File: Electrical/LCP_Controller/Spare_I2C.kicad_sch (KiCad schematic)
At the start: 4 parts, among them Q2 TSM500P02CX RFG

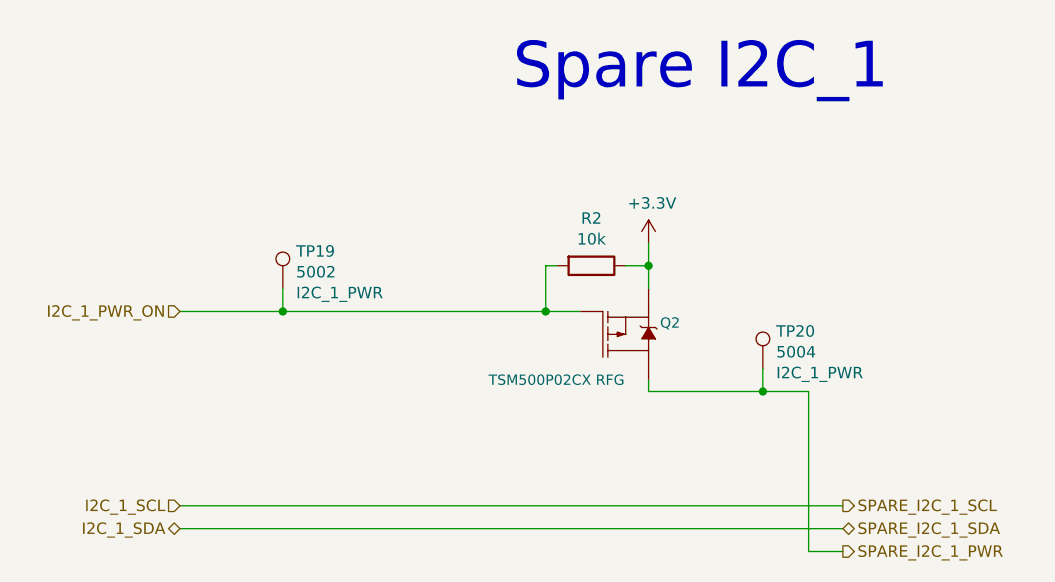
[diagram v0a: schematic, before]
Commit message: Hardware Revision : v0.3
1. modified schematic design, removed unnecessary test points.
2. pcb layout 2x8 Inches allowance dimension, layout is in progress
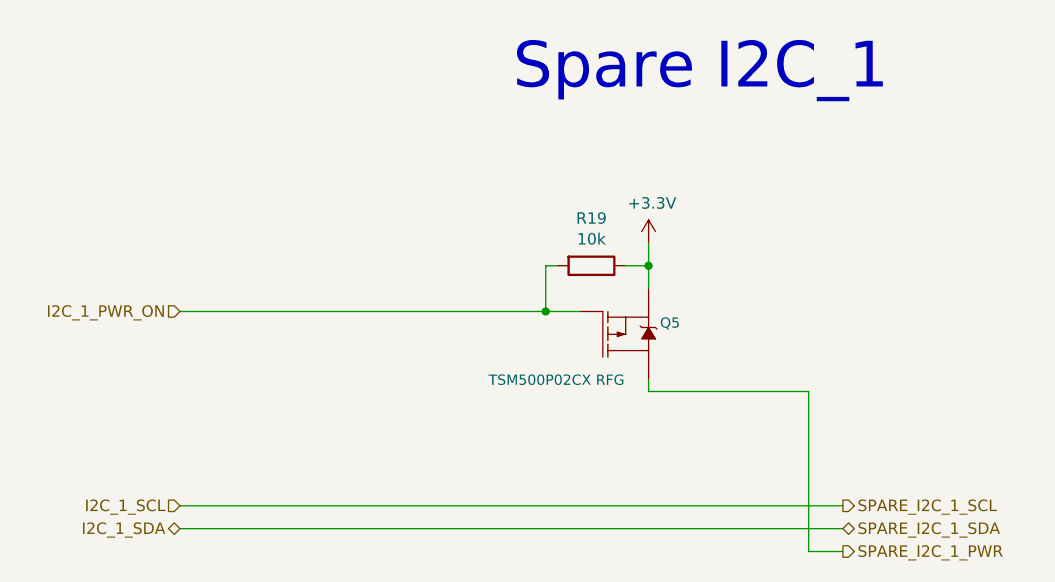
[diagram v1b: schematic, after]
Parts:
- removed TP19: 5002, TestPoint:TestPoint_Keystone_5000-5004_Miniature, symbol Connector:TestPoint
- removed TP20: 5004, TestPoint:TestPoint_Keystone_5000-5004_Miniature, symbol Connector:TestPoint
- renumbered Q2 to Q5, R2 to R19
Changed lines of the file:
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@@
   (junction (at 124.46 91.44) (diameter 0) (color 0 0 0 0)
-  )
-  (junction (at 95.25 91.44) (diameter 0) (color 0 0 0 0)
-  )
-  (junction (at 148.59 100.33) (diameter 0) (color 0 0 0 0)
   )
   (wire (pts (xy 153.67 100.33) (xy 153.67 118.11))
@@
     (stroke (width 0) (type default) (color 0 0 0 0))
   )
-  (wire (pts (xy 135.89 100.33) (xy 148.59 100.33))
+  (wire (pts (xy 135.89 100.33) (xy 153.67 100.33))
     (stroke (width 0) (type default) (color 0 0 0 0))
   )
-  (wire (pts (xy 95.25 91.44) (xy 124.46 91.44))
+  (wire (pts (xy 83.82 91.44) (xy 124.46 91.44))
     (stroke (width 0) (type default) (color 0 0 0 0))
   )
   (wire (pts (xy 157.48 118.11) (xy 153.67 118.11))
-    (stroke (width 0) (type default) (color 0 0 0 0))
-  )
-  (wire (pts (xy 148.59 97.79) (xy 148.59 100.33))
     (stroke (width 0) (type default) (color 0 0 0 0))
   )
@@
     (stroke (width 0) (type default) (color 0 0 0 0))
   )
-  (wire (pts (xy 83.82 91.44) (xy 95.25 91.44))
-    (stroke (width 0) (type default) (color 0 0 0 0))
-  )
-  (wire (pts (xy 148.59 100.33) (xy 153.67 100.33))
-    (stroke (width 0) (type default) (color 0 0 0 0))
-  )
   (wire (pts (xy 135.89 83.82) (xy 135.89 86.36))
     (stroke (width 0) (type default) (color 0 0 0 0))
   )
   (wire (pts (xy 124.46 86.36) (xy 125.73 86.36))
-    (stroke (width 0) (type default) (color 0 0 0 0))
-  )
-  (wire (pts (xy 95.25 88.9) (xy 95.25 91.44))
     (stroke (width 0) (type default) (color 0 0 0 0))
   )
@@
     (effects (font (size 1.27 1.27)) (justify right))
   )
-  (symbol (lib_id "Connector:TestPoint") (at 148.59 97.79 0) (unit 1)
-    (in_bom yes) (on_board yes)
-    (property "Reference" "TP20" (id 0) (at 150.0632 93.6498 0)
-      (effects (font (size 1.27 1.27)) (justify left))
-    )
-    (property "Value" "5004" (id 1) (at 150.0632 95.9612 0)
-      (effects (font (size 1.27 1.27)) (justify left))
-    )
-    (property "Footprint" "TestPoint:TestPoint_Keystone_5000-5004_Miniature" (id 2) (at 153.67 97.79 0)
-      (effects (font (size 1.27 1.27)) hide)
-    )
-    (property "Datasheet" "~" (id 3) (at 153.67 97.79 0)
-      (effects (font (size 1.27 1.27)) hide)
-    )
-    (property "TestPoint" "I2C_1_PWR" (id 4) (at 150.0632 98.2726 0)
-      (effects (font (size 1.27 1.27)) (justify left))
-    )
-    (property "MPN" "" (id 5) (at 148.59 97.79 0)
-      (effects (font (size 1.27 1.27)) hide)
-    )
-    (pin "1")
-  )
   (symbol (lib_id "SparkFun-DiscreteSemi:MOSFET_PCH-DMG2307L") (at 133.35 93.98 0) (mirror x) (unit 1)
     (in_bom yes) (on_board yes)
-    (property "Reference" "Q2" (id 0) (at 137.16 92.71 0)
+    (property "Reference" "Q5" (id 0) (at 137.16 92.71 0)
       (effects (font (size 1.143 1.143)) (justify left))
     )
@@
   (symbol (lib_id "power:+3.3V") (at 135.89 83.82 0) (unit 1)
     (in_bom yes) (on_board yes)
-    (property "Reference" "#PWR011" (id 0) (at 135.89 87.63 0)
+    (property "Reference" "#PWR059" (id 0) (at 135.89 87.63 0)
       (effects (font (size 1.27 1.27)) hide)
     )
@@
   (symbol (lib_id "Device:R") (at 129.54 86.36 270) (unit 1)
     (in_bom yes) (on_board yes)
-    (property "Reference" "R2" (id 0) (at 129.54 81.1022 90))
+    (property "Reference" "R19" (id 0) (at 129.54 81.1022 90))
     (property "Value" "10k" (id 1) (at 129.54 83.4136 90))
     (property "Footprint" "Resistor_SMD:R_0805_2012Metric" (id 2) (at 129.54 84.582 90)
@@
     (pin "2")
   )
-  (symbol (lib_id "Connector:TestPoint") (at 95.25 88.9 0) (unit 1)
-    (in_bom yes) (on_board yes)
-    (property "Reference" "TP19" (id 0) (at 96.7232 84.7598 0)
-      (effects (font (size 1.27 1.27)) (justify left))
-    )
-    (property "Value" "5002" (id 1) (at 96.7232 87.0712 0)
-      (effects (font (size 1.27 1.27)) (justify left))
-    )
-    (property "Footprint" "TestPoint:TestPoint_Keystone_5000-5004_Miniature" (id 2) (at 100.33 88.9 0)
-      (effects (font (size 1.27 1.27)) hide)
-    )
-    (property "Datasheet" "~" (id 3) (at 100.33 88.9 0)
-      (effects (font (size 1.27 1.27)) hide)
-    )
-    (property "TestPoint" "I2C_1_PWR" (id 4) (at 96.7232 89.3826 0)
-      (effects (font (size 1.27 1.27)) (justify left))
-    )
-    (property "MPN" "" (id 5) (at 95.25 88.9 0)
-      (effects (font (size 1.27 1.27)) hide)
-    )
-    (pin "1")
-  )
 )
